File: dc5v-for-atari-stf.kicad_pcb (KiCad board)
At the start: 2 copper layers, 0 parts

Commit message: pcb : layout, pcb edges
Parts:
- added D1: LED, LED_THT:LED_D3.0mm, F.Cu at (140.0, 85.0)
- added H1: M3, MountingHole:MountingHole_3.5mm, F.Cu at (98.0, 59.5)
- added H2: M3, MountingHole:MountingHole_3.5mm, F.Cu at (202.0, 59.5)
- added H3: M3, MountingHole:MountingHole_3.5mm, F.Cu at (204.5, 139.5)
- added H4: M3, MountingHole:MountingHole_3.5mm, F.Cu at (95.5, 139.5)
- added J1: Conn_01x02, commons-interconnect_THT:Fixed_Terminal_Blocks_Wurth_Elektronik_Serie_4122_7.00mm_Screwless_45degrees_1x02, F.Cu at (113.5, 65.0)
- added J2: Conn_01x06, Connector_PinHeader_2.54mm:PinHeader_1x06_P2.54mm_Vertical, F.Cu at (200.5, 130.5)
- added J3: Adjustable MT3608 module, assemblies_power_modules:module_mt3608_ajustable_output, F.Cu at (184.0, 100.0)
- added J4: Fixed 12V module, assemblies_power_modules:module_dc_dc_step_up_12V_W10.16mm_H20.5mm_PinSocket_1x04_P2.54mm_Horizontal, F.Cu at (200.0, 115.1)
- added J5: Conn_01x02, Connector_PinHeader_2.54mm:PinHeader_1x02_P2.54mm_Vertical, F.Cu at (202.5, 72.5)
- added R1: 2K, commons-passives_THT:Passive_THT_resistor_W2.54mm_L12.70mm, F.Cu at (127.5, 85.0)
- added SW1: Momentary or Latched, commons-interconnect_THT:combined_push_button_4pins_X_latched_button_6pins__2rows_W5_6mm_pitch_2.5_2.6mm, F.Cu at (110.0, 85.0)
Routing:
- net +12V: track 0.00 -> 49.0 mm
- net Net-(R1-Pad1): track 0.00 -> 13.9 mm
- net Net-(D1-Pad2): track 0.00 -> 3.61 mm
- added copper zone on F.Cu, net +5V
- added copper zone on B.Cu, net GND
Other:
- board outline added: 135 x 90 mm

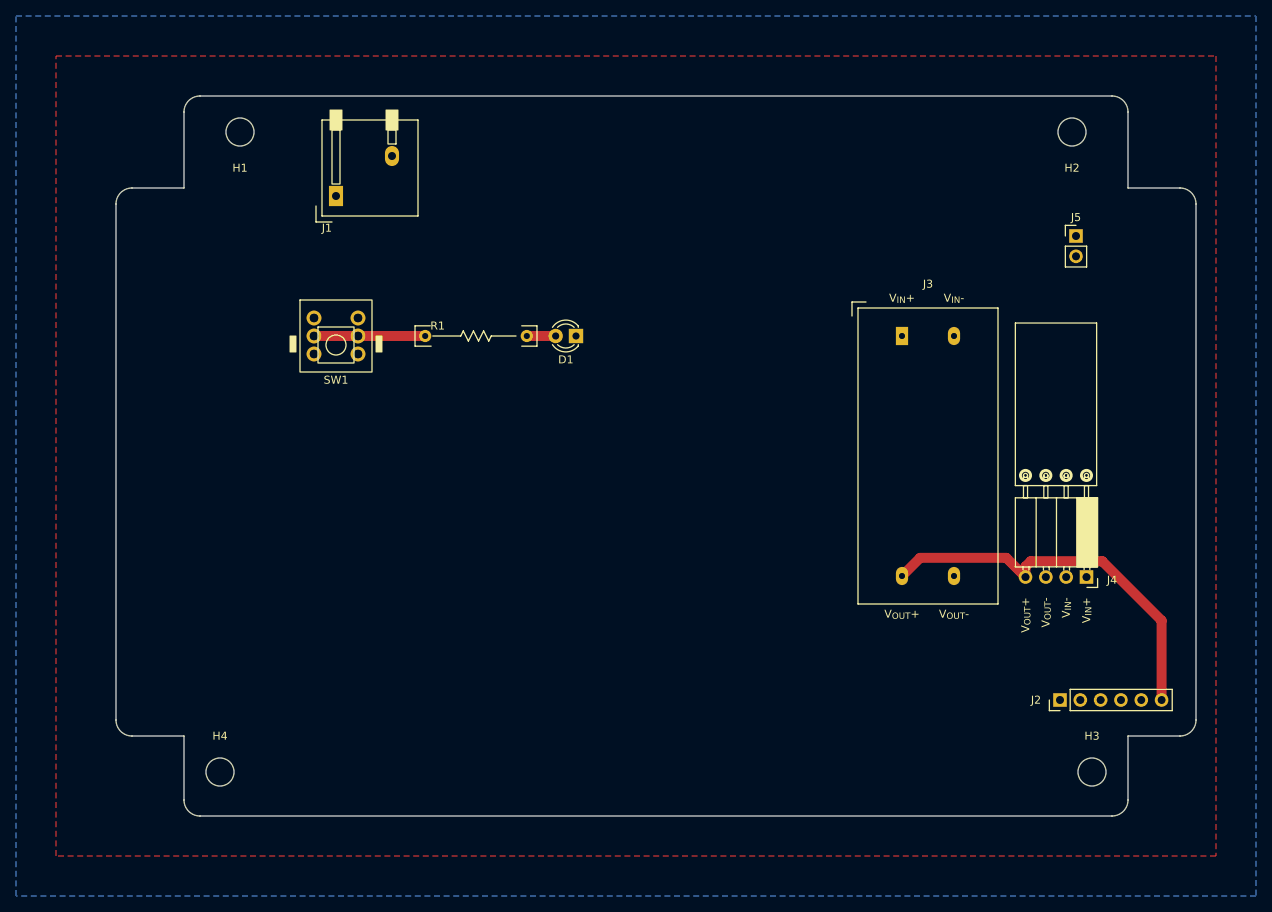
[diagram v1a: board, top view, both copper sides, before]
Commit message: pcb : label to show polarisation/voltages
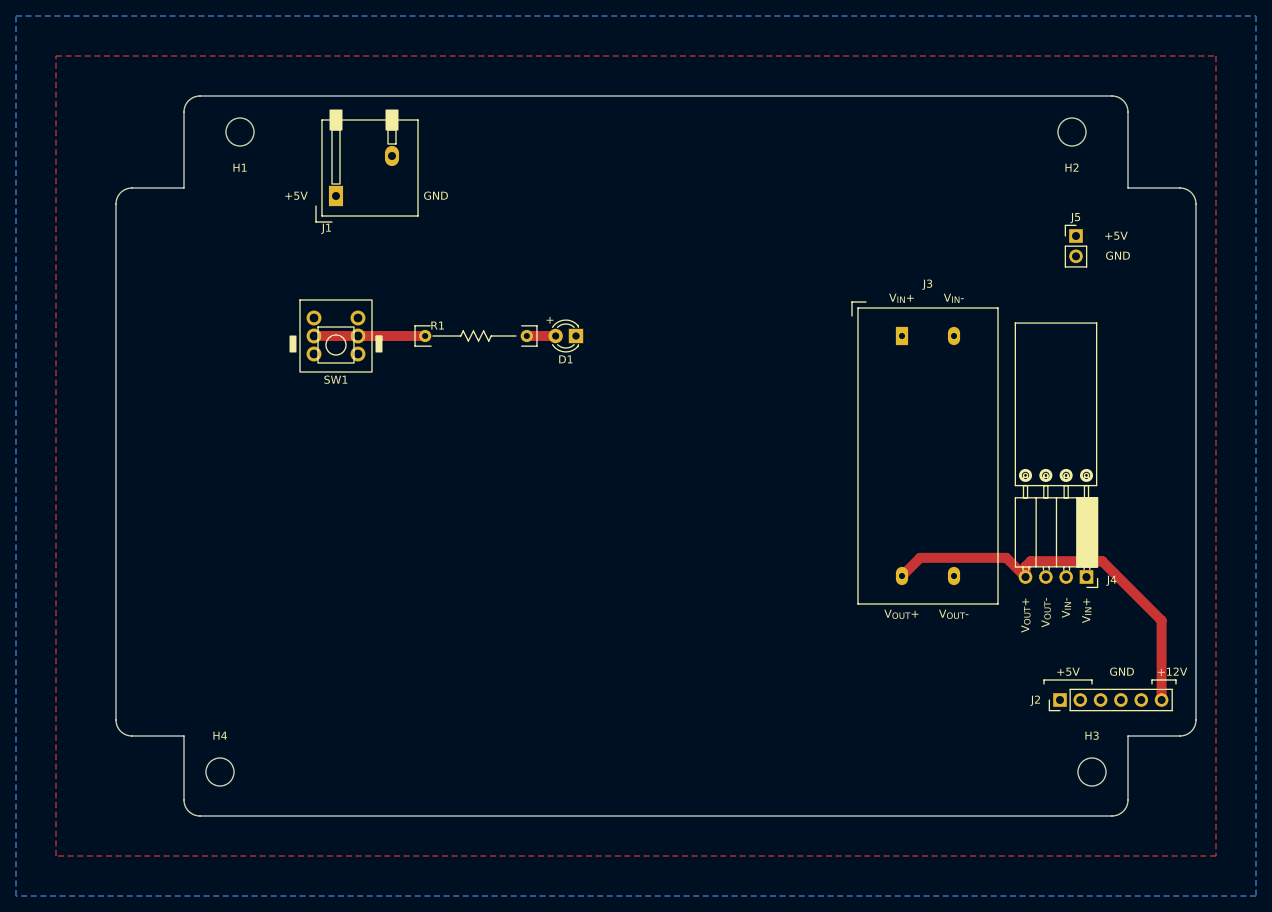
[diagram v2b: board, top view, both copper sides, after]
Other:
- board text added: "+"
- board text added: "+12V"
- board text added: "+5V"
- board text added: "GND"
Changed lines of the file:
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@@
     (pad "" np_thru_hole circle (at 0 0) (size 3.5 3.5) (drill 3.5) (layers *.Cu *.Mask))
   )
+  (gr_line (start 198.5 128) (end 204.5 128) (layer "F.SilkS") (width 0.15))
+  (gr_line (start 204.5 128) (end 204.5 128.5) (layer "F.SilkS") (width 0.15))
+  (gr_line (start 198.5 128.5) (end 198.5 128) (layer "F.SilkS") (width 0.15))
+  (gr_line (start 215 128.5) (end 215 128) (layer "F.SilkS") (width 0.15))
+  (gr_line (start 212 128.5) (end 212 128) (layer "F.SilkS") (width 0.15))
+  (gr_line (start 215 128) (end 212 128) (layer "F.SilkS") (width 0.15))
   (gr_line (start 95 139.5) (end 96 139.5) (layer "Dwgs.User") (width 0.15))
   (gr_line (start 205 139.5) (end 204 139.5) (layer "Dwgs.User") (width 0.15))
@@
   (gr_arc (start 91 57) (mid 91.585786 55.585786) (end 93 55) (layer "Edge.Cuts") (width 0.1))
   (gr_line (start 93 145) (end 207 145) (layer "Edge.Cuts") (width 0.1))
+  (gr_text "GND" (at 208.25 127) (layer "F.SilkS")
+    (effects (font (size 1 1) (thickness 0.15)))
+  )
+  (gr_text "+5V" (at 207.5 72.5) (layer "F.SilkS")
+    (effects (font (size 1 1) (thickness 0.15)))
+  )
+  (gr_text "+5V" (at 201.5 127) (layer "F.SilkS")
+    (effects (font (size 1 1) (thickness 0.15)))
+  )
+  (gr_text "+5V" (at 105 67.5) (layer "F.SilkS")
+    (effects (font (size 1 1) (thickness 0.15)))
+  )
+  (gr_text "GND" (at 122.5 67.5) (layer "F.SilkS")
+    (effects (font (size 1 1) (thickness 0.15)))
+  )
+  (gr_text "+12V" (at 214.5 127) (layer "F.SilkS")
+    (effects (font (size 1 1) (thickness 0.15)))
+  )
+  (gr_text "+" (at 136.75 83) (layer "F.SilkS")
+    (effects (font (size 1 1) (thickness 0.15)))
+  )
+  (gr_text "GND" (at 207.75 75) (layer "F.SilkS")
+    (effects (font (size 1 1) (thickness 0.15)))
+  )
   (segment (start 133.85 85) (end 137.46 85) (width 1.25) (layer "F.Cu") (net 2))
   (segment (start 205.784511 113.155489) (end 196.844511 113.155489) (width 1.25) (layer "F.Cu") (net 4))

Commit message: pcb : rework using updates
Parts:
- added F1: Fuse, commons-passives_THT:FuseHolder_Cylinder_5x20mm_Wurth_Elektronik_696310001002, F.Cu at (116.4, 85.0)
- J1: value Conn_01x02 -> Conn_01x03; footprint commons-interconnect_THT:Fixed_Terminal_Blocks_Wurth_Elektronik_Serie_4122_7.00mm_Screwless_45degrees_1x02 -> commons-interconnect_THT:Fixed_Terminal_Blocks_Wurth_Elektronik_Serie_4122_7.00mm_Screwless_45degrees_1x03
- moved D1 15.0 mm to (140.0, 100.0)
- moved R1 15.0 mm to (127.5, 100.0)
- moved SW1 15.0 mm to (110.0, 100.0)
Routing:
- net Net-(F1-Pad2): track 0.00 -> 19.2 mm
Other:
- board text added: "+5V NO FUSE"
- board text added: "+5V THROUGH FUSE"
